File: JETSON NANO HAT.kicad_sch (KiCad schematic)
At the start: 12 parts, among them J1 CAMARRAY, J2 OUTPUTS, J4 INPUTS

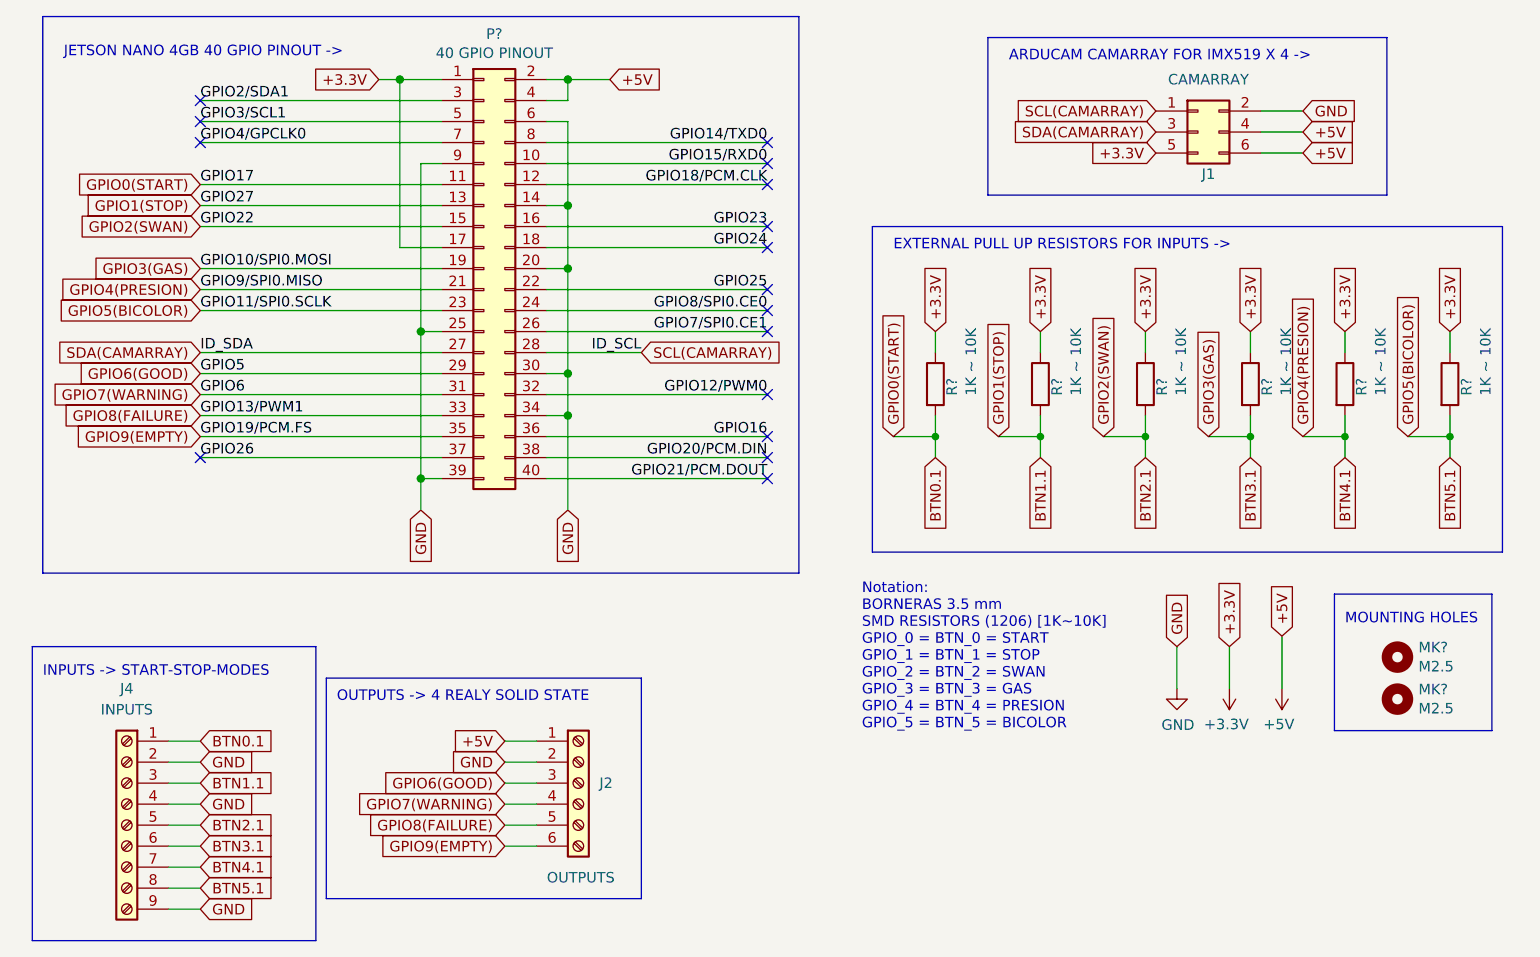
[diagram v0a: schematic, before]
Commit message: new input added : 7 inputs 4 outputs & .sch - .pcb updated
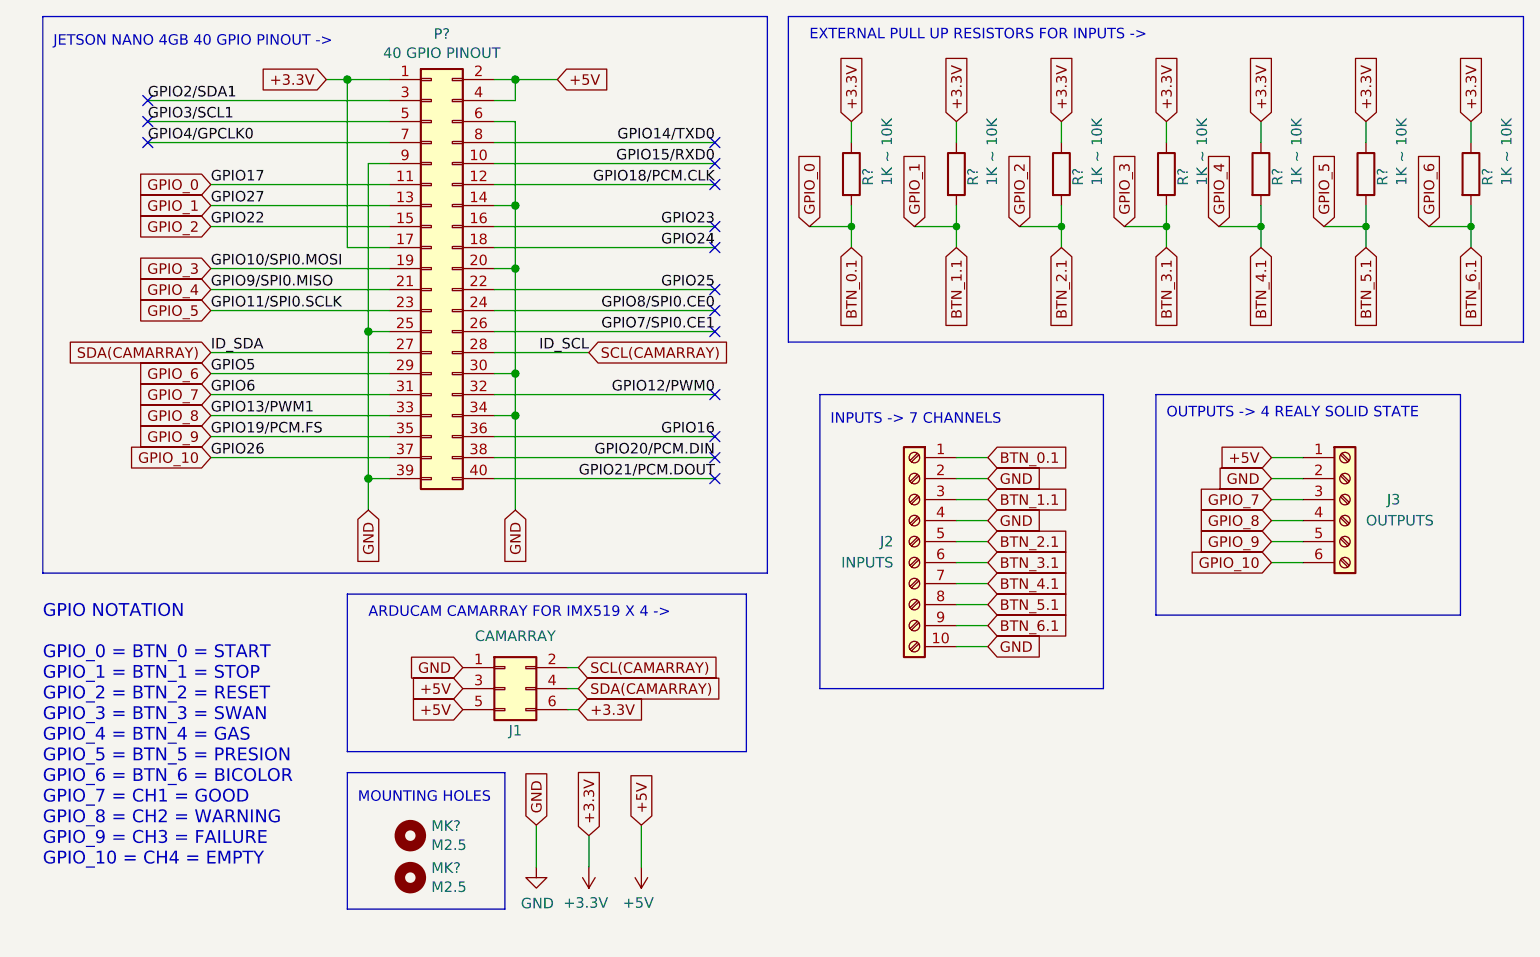
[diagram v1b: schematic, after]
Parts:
- removed J4: INPUTS, TerminalBlock_Phoenix:TerminalBlock_Phoenix_PT-1,5-9-3.5-H_1x09_P3.50mm_Horizontal, symbol Connector:Screw_Terminal_01x09
- added J2: INPUTS, TerminalBlock_Phoenix:TerminalBlock_Phoenix_PT-1,5-10-3.5-H_1x10_P3.50mm_Horizontal, symbol Connector:Screw_Terminal_01x10
- added R?: 1K ~ 10K, Resistor_SMD:R_1206_3216Metric, symbol Device:R
- J1: footprint Connector_PinSocket_2.54mm:PinSocket_2x03_P2.54mm_Vertical -> Connector_PinHeader_2.54mm:PinHeader_2x03_P2.54mm_Vertical
- renumbered J2 to J3
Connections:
- net +3V3: now also J1.6 (Pin_6), R?.1; no longer J1.5 (Pin_5)
- net +5V: now also J1.3 (Pin_3), J1.5 (Pin_5); no longer J1.4 (Pin_4), J1.6 (Pin_6)
- net GND: now also J1.1 (Pin_1), J2.10 (Pin_10), J2.2 (Pin_2), J2.4 (Pin_4); no longer J1.2 (Pin_2)
- net SCL(CAMARRAY): now also J1.2 (Pin_2); no longer J1.1 (Pin_1)
- net SDA(CAMARRAY): now also J1.4 (Pin_4); no longer J1.3 (Pin_3)
- net BTN0.1 renamed BTN_0.1
- net BTN_0.1: now also J2.1 (Pin_1)
- net BTN1.1 renamed BTN_1.1
- net BTN_1.1: now also J2.3 (Pin_3)
- net BTN2.1 renamed BTN_2.1
- net BTN_2.1: now also J2.5 (Pin_5)
- net BTN3.1 renamed BTN_3.1
- net BTN_3.1: now also J2.6 (Pin_6)
- net BTN4.1 renamed BTN_4.1
- net BTN_4.1: now also J2.7 (Pin_7)
- net BTN5.1 renamed BTN_5.1
- net BTN_5.1: now also J2.8 (Pin_8)
- net GPIO26 renamed GPIO_10
- net GPIO_10: now also J3.6 (Pin_6)
- net GPIO6(GOOD) renamed BTN_6.1
- net BTN_6.1: now also J2.9 (Pin_9), R?.2; no longer J3.3 (Pin_3)
- net GPIO7(WARNING) renamed GPIO_7
- net GPIO_7: now also J3.3 (Pin_3); no longer J3.4 (Pin_4)
- net GPIO8(FAILURE) renamed GPIO_8
- net GPIO_8: now also J3.4 (Pin_4); no longer J3.5 (Pin_5)
- net GPIO9(EMPTY) renamed GPIO_9
- net GPIO_9: now also J3.5 (Pin_5); no longer J3.6 (Pin_6)
- no-connect marks 16 -> 15
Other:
- note added: "GPIO NOTATION GPIO_0 = BTN_0 = START GPIO_1 = BTN_1 = STOP GPIO_2 = BTN_2 = RESET GPIO_3 = BTN_3 = SWAN GPIO_4 = BTN_4 = GAS GPIO_5 = BTN_5 = PRESION GPIO_6 = BTN_6 = BICOLOR GPIO_7 = CH1 = GOOD GPIO_8 = CH2 = WARNING GPIO_9 = CH3 = FAILURE GPIO_10 = CH4 = EMPTY"
- note added: "INPUTS -> 7 CHANNELS"
- note removed: "INPUTS -> START-STOP-MODES"
- note removed: "Notation: BORNERAS 3.5 mm SMD RESISTORS (1206) [1K~10K] GPIO_0 = BTN_0 = START GPIO_1 = BTN_1 = STOP GPIO_2 = BTN_2 = SWAN GPIO_3 = BTN_3 = GAS GPIO_4 = BTN_4 = PRESION GPIO_5 = BTN_5 = BICOLOR"
- moved on the sheet: J1, J3, MK?, P?, R?
